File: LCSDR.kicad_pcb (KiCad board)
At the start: 2 copper layers, 150 x 95 mm, 112 parts, among them J1 MIC_PTT, J10 Conn_01x01, J11 Conn_01x01, J12 USB_B_Mini, J13 Jack-DC, J14 I2C, J15 IO, J2 IDC10 Serial Wire, J3 Audio-Jack-3_2Switches, J4 LINEIN, J5 IQ_IN, J6 IQ_OUT, J7 CLK, J8 Conn_01x01, J9 Conn_01x01, Q1 2N7002, U1 SI5351A, U16 WM8731_alt, U2 FM24CL16B, U3 STM32F401RCTx, U4 AP1117-33, U5 MC34063, U6 MC34063, U7 78M09, U8 4053, U9 4053, Y1 20Mhz, Y2 Crystal

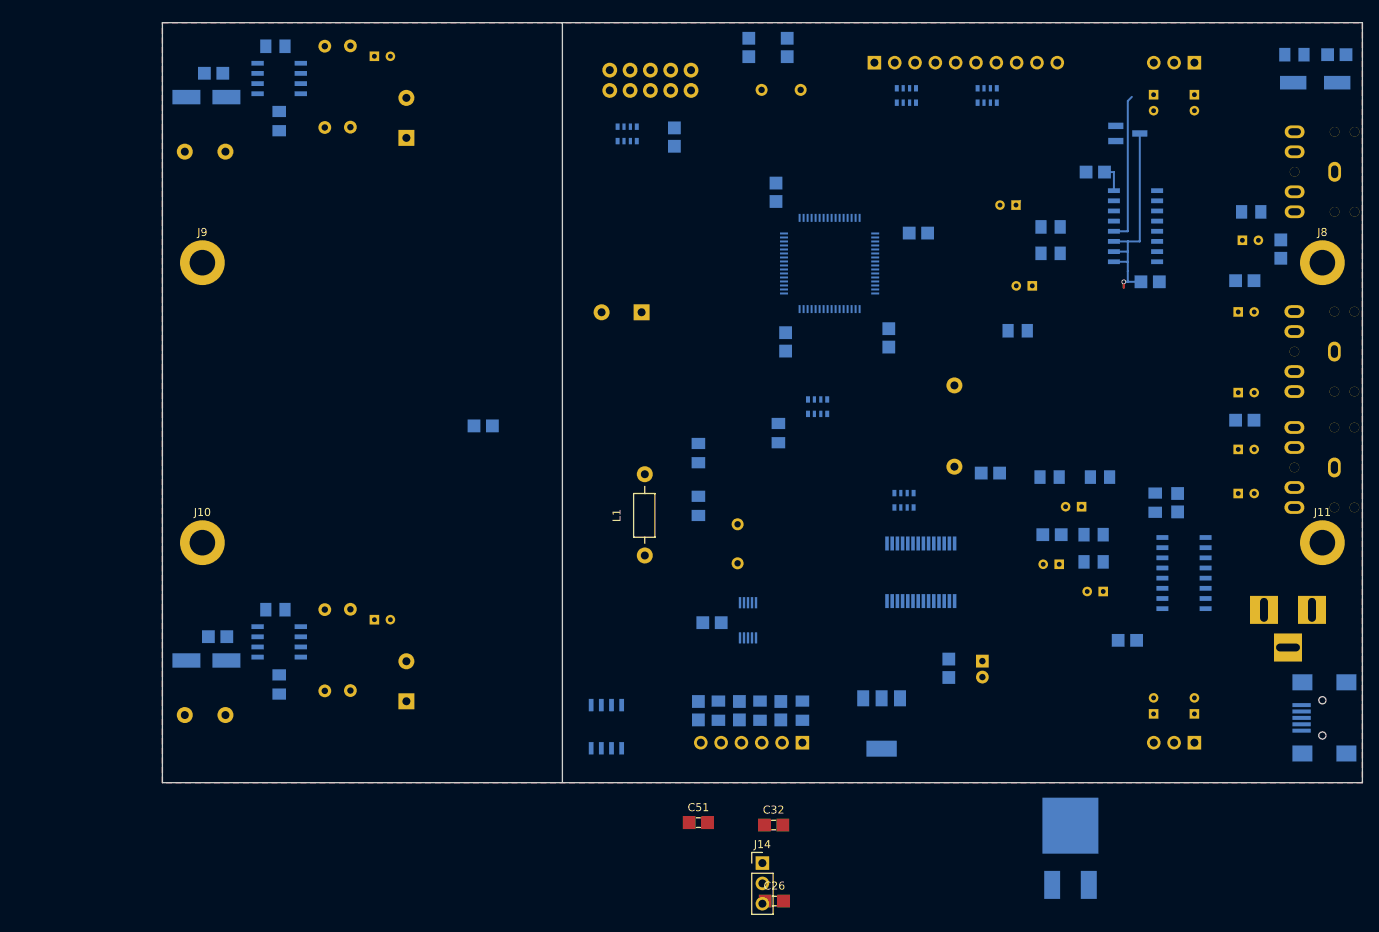
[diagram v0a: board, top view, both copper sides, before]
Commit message: TODO: power supplay connector
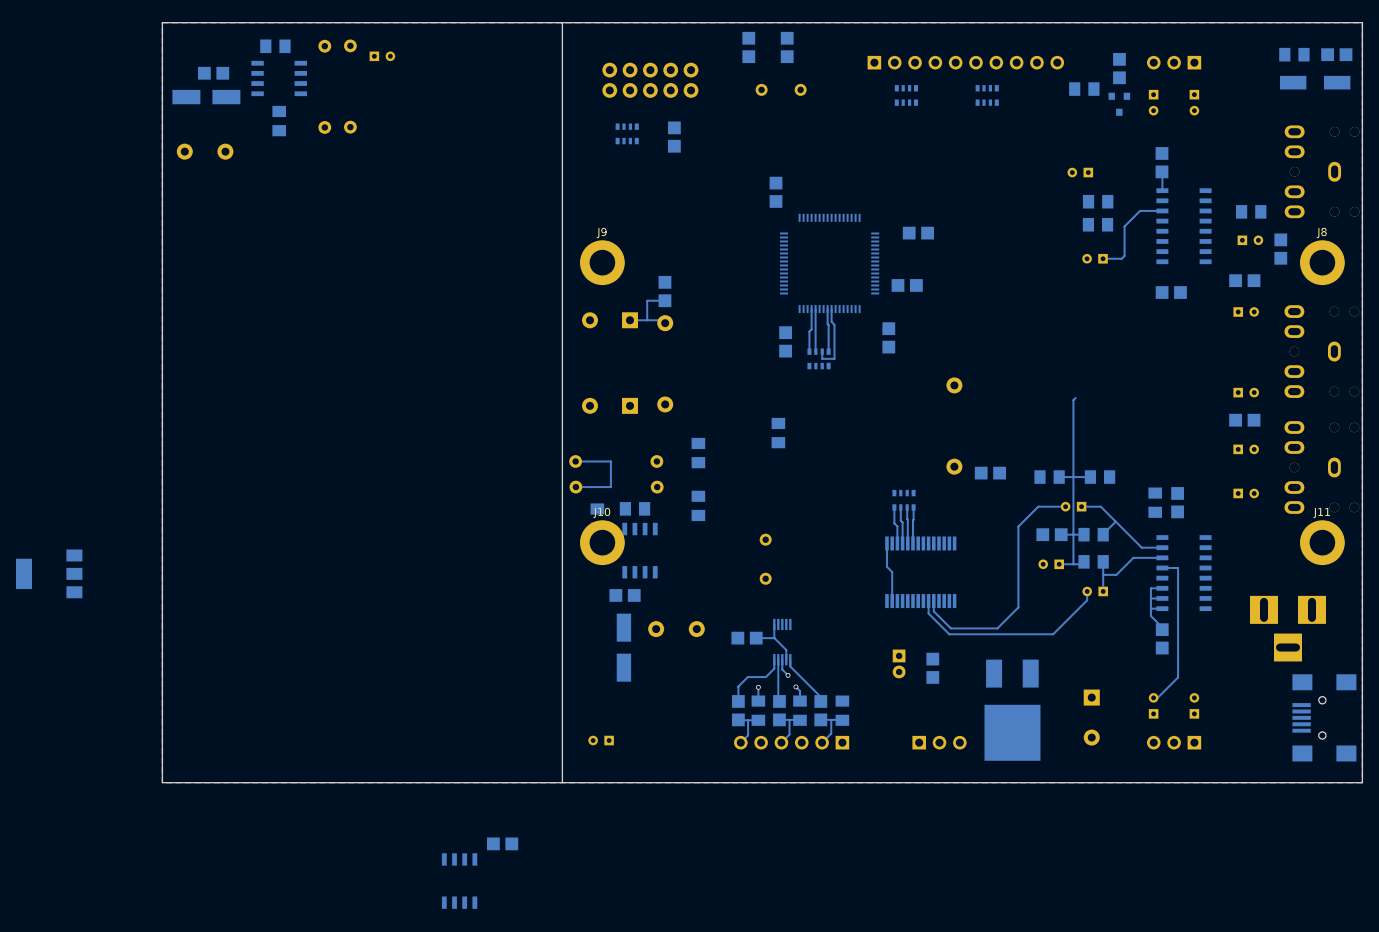
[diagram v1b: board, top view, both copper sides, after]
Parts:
- C26, C32, C51, J14, L1: moved to B.Cu
- Q1: footprint TO_SOT_Packages_SMD:SOT-23_Handsoldering -> TO_SOT_Packages_SMD:SOT-23
- moved C39 110.6 mm to (181.2, 124.4), turned to 270 degrees
- moved C51 108.0 mm to (184.6, 45.7), turned to 90 degrees
- moved U4 105.7 mm to (50.9, 108.9), turned to 180 degrees
- moved C26 77.4 mm to (127.8, 73.6), turned to 90 degrees
- moved C32 69.5 mm to (158.1, 72.8)
- moved L2 59.9 mm to (126.7, 120.9)
- moved C27 52.3 mm to (107.5, 142.7)
- moved D2 52.2 mm to (122.7, 118.1), turned to 270 degrees
- moved C40 51.2 mm to (122.8, 111.6)
- moved J10 50.0 mm to (120.0, 105.0)
- moved J9 50.0 mm to (120.0, 70.0)
- moved R15 49.6 mm to (124.1, 100.8), turned to 180 degrees
- moved R11 48.7 mm to (126.8, 98.0), turned to 180 degrees
- moved U5 46.5 mm to (124.7, 106.0), turned to 90 degrees
- moved C38 46.3 mm to (123.5, 87.9), turned to 180 degrees
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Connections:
- RN3 pad 4: (no net) -> IO0
- U3 pad 8: (no net) -> IO0
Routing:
- net Net-(C56-Pad1): track 0.00 -> 30.9 mm
- net LINE_IN_RIGHT: track 0.00 -> 30.9 mm
- net LINE_IN_LEFT: track 0.00 -> 25.3 mm
- net +3V3: track 0.00 -> 24.0 mm
- net Net-(C16-Pad2): track 0.00 -> 19.8 mm
- net Net-(C21-Pad1): track 28.9 -> 10.0 mm, vias 1 -> 0
- net Net-(C14-Pad2): track 18.7 -> 0.00 mm
- net Net-(C52-Pad1): track 0.00 -> 14.5 mm
- net Net-(C55-Pad1): track 0.00 -> 12.1 mm
- net +12V: track 0.00 -> 12.0 mm
- net Net-(C53-Pad1): track 0.00 -> 12.0 mm
- net I2C_SDA_MCU: track 0.00 -> 8.80 mm
- net Net-(C4-Pad2): track 0.00 -> 8.41 mm
- net Net-(C2-Pad2): track 0.00 -> 6.81 mm
- net CLK2: track 0.00 -> 6.05 mm
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
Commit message: add I2S_CLKIN_MCU
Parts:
- removed C14, C15, C16, C52, C53, C54, C55, C8: 1uF, Capacitors_ThroughHole:CP_Radial_D4.0mm_P2.00mm
- removed C21, C48: 22..47nF, UI:C_1206_0603
- removed C25: 330uF, Capacitors_ThroughHole:CP_Radial_D10.0mm_P5.00mm
- removed C31, C47, C56: 100nF, UI:C_1206_0603
- removed C37, C57: 10uF, Capacitors_ThroughHole:CP_Radial_D4.0mm_P2.00mm
- removed C39: 1000uF, Capacitors_ThroughHole:CP_Radial_D10.0mm_P5.00mm
- removed C51: 15nF, UI:C_1206_0603
- removed J12: USB_B_Mini, Connect:USB_Mini-B
- removed J14: I2C, Pin_Headers:Pin_Header_Straight_1x03_Pitch2.54mm
- removed J15: IO, Pin_Headers:Pin_Header_Straight_1x10_Pitch2.54mm
- removed J7: CLK, Pin_Headers:Pin_Header_Straight_1x06_Pitch2.54mm
- removed L1: 280uH, Choke_Axial_ThroughHole:Choke_Horizontal_RM10mm
- removed Q1: 2N7002, TO_SOT_Packages_SMD:SOT-23
- removed R14: 1k, UI:R_1206_0603
- removed R16: 6.2k, UI:R_1206_0603
- removed R17, R22, R23, R26, R27: 10k, UI:R_1206_0603
- removed R18: 2.2k, UI:R_1206_0603
- removed R19: 100, UI:R_1206_0603
- removed R75, R76: 4.7k, UI:R_1206_0603
- removed RN1: 47, Resistors_SMD:R_Array_Convex_4x0603
- removed U4: AP1117-33, TO_SOT_Packages_SMD:SOT-223
- removed U6: MC34063, UI:SOIC-8_3.9x4.9mm_Pitch1.27mm
- removed U8, U9: 4053, Housings_SOIC:SOIC-16_3.9x9.9mm_Pitch1.27mm
- added RN5, RN6, RN8: 47, Resistors_SMD:R_Array_Convex_4x0603, F.Cu at (140.0, 145.1)
- C36: footprint Capacitors_ThroughHole:CP_Radial_D4.0mm_P2.00mm -> Capacitors_THT:CP_Radial_D6.3mm_P2.50mm
- C5, C6: value 1uF -> 22pF; footprint Capacitors_ThroughHole:CP_Radial_D4.0mm_P2.00mm -> UI:C_1206_0603; moved to F.Cu
- J2: value IDC10 Serial Wire -> Conn_01x30; footprint UI:USBBLASTER -> Pin_Headers:Pin_Header_Straight_1x30_Pitch2.54mm
- J4: value LINEIN -> Conn_01x30; footprint UI:audio_jack_3_5mm_PJ307 -> Pin_Headers:Pin_Header_Straight_1x30_Pitch2.54mm
- J5: value IQ_IN -> USB_B_Mini; footprint Pin_Headers:Pin_Header_Straight_1x03_Pitch2.54mm -> Connectors:USB_Mini-B
- J6: value IQ_OUT -> IDC10 Serial Wire; footprint Pin_Headers:Pin_Header_Straight_1x03_Pitch2.54mm -> UI:USBBLASTER; moved to F.Cu
- R5, R6: value 10k -> 4.7k; moved to F.Cu
- RN4: moved to F.Cu
- moved J6 113.7 mm to (140.0, 145.1), turned to 0 degrees
- moved J4 97.8 mm to (129.0, 43.0), turned to 270 degrees
- moved J2 84.9 mm to (129.0, 132.0), turned to 270 degrees
- moved C5 78.8 mm to (140.0, 145.1)
- moved C6 75.3 mm to (140.0, 145.1)
- moved R5 66.6 mm to (140.0, 145.1), turned to 0 degrees
- moved RN4 63.4 mm to (140.0, 145.1), turned to 0 degrees
- moved R6 56.0 mm to (140.0, 145.1)
- moved J10 26.0 mm to (119.0, 131.0)
- moved J11 26.0 mm to (211.0, 131.0)
- moved J8 26.0 mm to (211.0, 44.0)
- moved J9 26.0 mm to (119.0, 44.0)
- moved R4 23.9 mm to (184.0, 52.0)
- moved D1 22.4 mm to (188.0, 55.0)
- moved C7 20.1 mm to (193.0, 51.0)
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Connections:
- C38 pad 1: Net-(C38-Pad1) -> +3V3
- C5 pad 1: Net-(C5-Pad1) -> GND
- C6 pad 2: Net-(C6-Pad2) -> GND
- J2 pad 1: +3V3 -> GND
- J2 pad 2: Net-(J2-Pad2) -> CLK2
- J2 pad 4: Net-(J2-Pad4) -> CLK1
- J2 pad 6: Net-(J2-Pad6) -> CLK0
- J2 pad 7: (no net) -> Net-(J2-Pad7)
- J2 pad 8: (no net) -> Net-(J2-Pad8)
- J2 pad 9: GND -> Net-(J2-Pad9)
- J3 pad 4: (no net) -> Net-(J3-Pad4)
- J3 pad 5: (no net) -> Net-(J3-Pad5)
- J4 pad 1: Net-(C6-Pad2) -> Net-(J4-Pad1)
- J4 pad 10: (no net) -> GND
- J4 pad 2: Net-(C5-Pad2) -> Net-(J4-Pad2)
- J4 pad 3: GND -> Net-(J4-Pad3)
- J4 pad 4: Net-(C6-Pad2) -> Net-(J4-Pad4)
- J4 pad 5: Net-(C5-Pad2) -> Net-(J4-Pad5)
- J4 pad 6: (no net) -> Net-(J4-Pad6)
- J4 pad 7: (no net) -> Net-(J4-Pad7)
- J4 pad 8: (no net) -> Net-(J4-Pad8)
- J4 pad 9: (no net) -> ADC
- J5 pad 1: I_IN -> Net-(J5-Pad1)
- J5 pad 2: GND -> Net-(J5-Pad2)
- J5 pad 3: Q_IN -> Net-(J5-Pad3)
- J6 pad 1: I_OUT -> MCU_VOLTAGE_33V
- J6 pad 2: GND -> Net-(J6-Pad2)
- J6 pad 3: Q_OUT -> GND
- L2 pad 2: Net-(C38-Pad1) -> +3V3
- R12 pad 2: +12V -> Net-(R12-Pad2)
- R15 pad 1: Net-(C38-Pad1) -> +3V3
- R5 pad 1: +9V -> +3V3
- R5 pad 2: Net-(C21-Pad1) -> I2C_SDA
- R6 pad 1: Net-(C56-Pad1) -> +3V3
- R6 pad 2: Net-(C53-Pad1) -> I2C_SCL
- RN2 pad 1: (no net) -> IO7
- RN2 pad 2: (no net) -> IO6
- RN2 pad 3: (no net) -> IO5
- RN2 pad 4: (no net) -> IO4
- RN3 pad 1: (no net) -> IO3
- RN3 pad 2: (no net) -> IO2
- RN3 pad 3: (no net) -> IO1
- RN4 pad 1: I2C_SCL -> IO3
- RN4 pad 2: I2C_SDA -> IO2
- RN4 pad 3: Net-(J12-Pad2) -> IO1
- RN4 pad 4: Net-(J12-Pad3) -> IO0
- RN4 pad 5: USB_DP -> Net-(J4-Pad1)
- RN4 pad 6: USB_DM -> Net-(J4-Pad2)
- RN4 pad 7: I2C_SDA_MCU -> Net-(J4-Pad3)
- RN4 pad 8: I2C_SCL_MCU -> Net-(J4-Pad4)
- U16 pad 2: (no net) -> CLKOUT_WM8731
- U16 pad 25: Net-(R19-Pad1) -> Net-(C6-Pad1)
- U16 pad 26: (no net) -> Net-(C5-Pad2)
- U2 pad 1: (no net) -> Net-(U2-Pad1)
- U2 pad 2: (no net) -> Net-(U2-Pad2)
- U2 pad 3: (no net) -> Net-(U2-Pad3)
- U3 pad 1: (no net) -> Net-(U3-Pad1)
- U3 pad 10: (no net) -> BAND2
- U3 pad 11: (no net) -> BAND3
- U3 pad 13: (no net) -> Net-(U3-Pad13)
- U3 pad 14: (no net) -> ATT
- U3 pad 15: (no net) -> PREAMP
- U3 pad 16: (no net) -> Net-(U3-Pad16)
- U3 pad 17: (no net) -> Net-(U3-Pad17)
- U3 pad 2: (no net) -> KEY_B
- U3 pad 20: (no net) -> Net-(U3-Pad20)
- U3 pad 21: (no net) -> TX1
- U3 pad 22: (no net) -> ENCODER_A
- U3 pad 23: (no net) -> ENCODER_B
- U3 pad 25: (no net) -> Net-(U3-Pad25)
- U3 pad 26: (no net) -> Net-(U3-Pad26)
- U3 pad 27: (no net) -> Net-(U3-Pad27)
- U3 pad 28: (no net) -> Net-(U3-Pad28)
- U3 pad 29: (no net) -> Net-(U3-Pad29)
- U3 pad 3: (no net) -> KEY_C
- U3 pad 38: (no net) -> Net-(U3-Pad38)
- U3 pad 4: (no net) -> KEY_D
- U3 pad 42: (no net) -> Net-(U3-Pad42)
- U3 pad 43: (no net) -> Net-(U3-Pad43)
- U3 pad 50: (no net) -> LCD_CE
- U3 pad 51: (no net) -> LCD_CLK
- U3 pad 52: (no net) -> LCD_DC
- U3 pad 53: (no net) -> LCD_DIN
- U3 pad 54: (no net) -> Net-(U3-Pad54)
- U3 pad 56: (no net) -> LCD_LIGHT
- U3 pad 57: (no net) -> I_IN_M2
- U3 pad 58: (no net) -> Q_IN_M1
- U3 pad 59: (no net) -> Q_IN_M2
- U3 pad 61: (no net) -> Net-(U3-Pad61)
- U3 pad 62: (no net) -> Net-(U3-Pad62)
- U3 pad 9: (no net) -> BAND1
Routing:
- net (no net): track 0.00 -> 87.2 mm
- net Net-(C56-Pad1): track 30.9 -> 0.00 mm
- net Net-(C16-Pad2): track 19.8 -> 0.00 mm
- net Net-(C52-Pad1): track 14.5 -> 0.00 mm
- net Net-(C55-Pad1): track 12.1 -> 0.00 mm
- net Net-(C53-Pad1): track 12.0 -> 0.00 mm
- net Net-(C21-Pad1): track 10.0 -> 0.00 mm
- net I2C_SDA_MCU: track 8.80 -> 0.00 mm
- net USB_DP: track 5.43 -> 0.00 mm
- net I2C_SCL_MCU: track 5.37 -> 0.00 mm
- net USB_DM: track 5.33 -> 0.00 mm
- net +9V: track 2.37 -> 0.00 mm
